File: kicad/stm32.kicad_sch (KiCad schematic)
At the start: 21 parts, among them U1 STM32L452REI6, X1 NX2012SA-32.768KHZ-EXS00A-MU0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

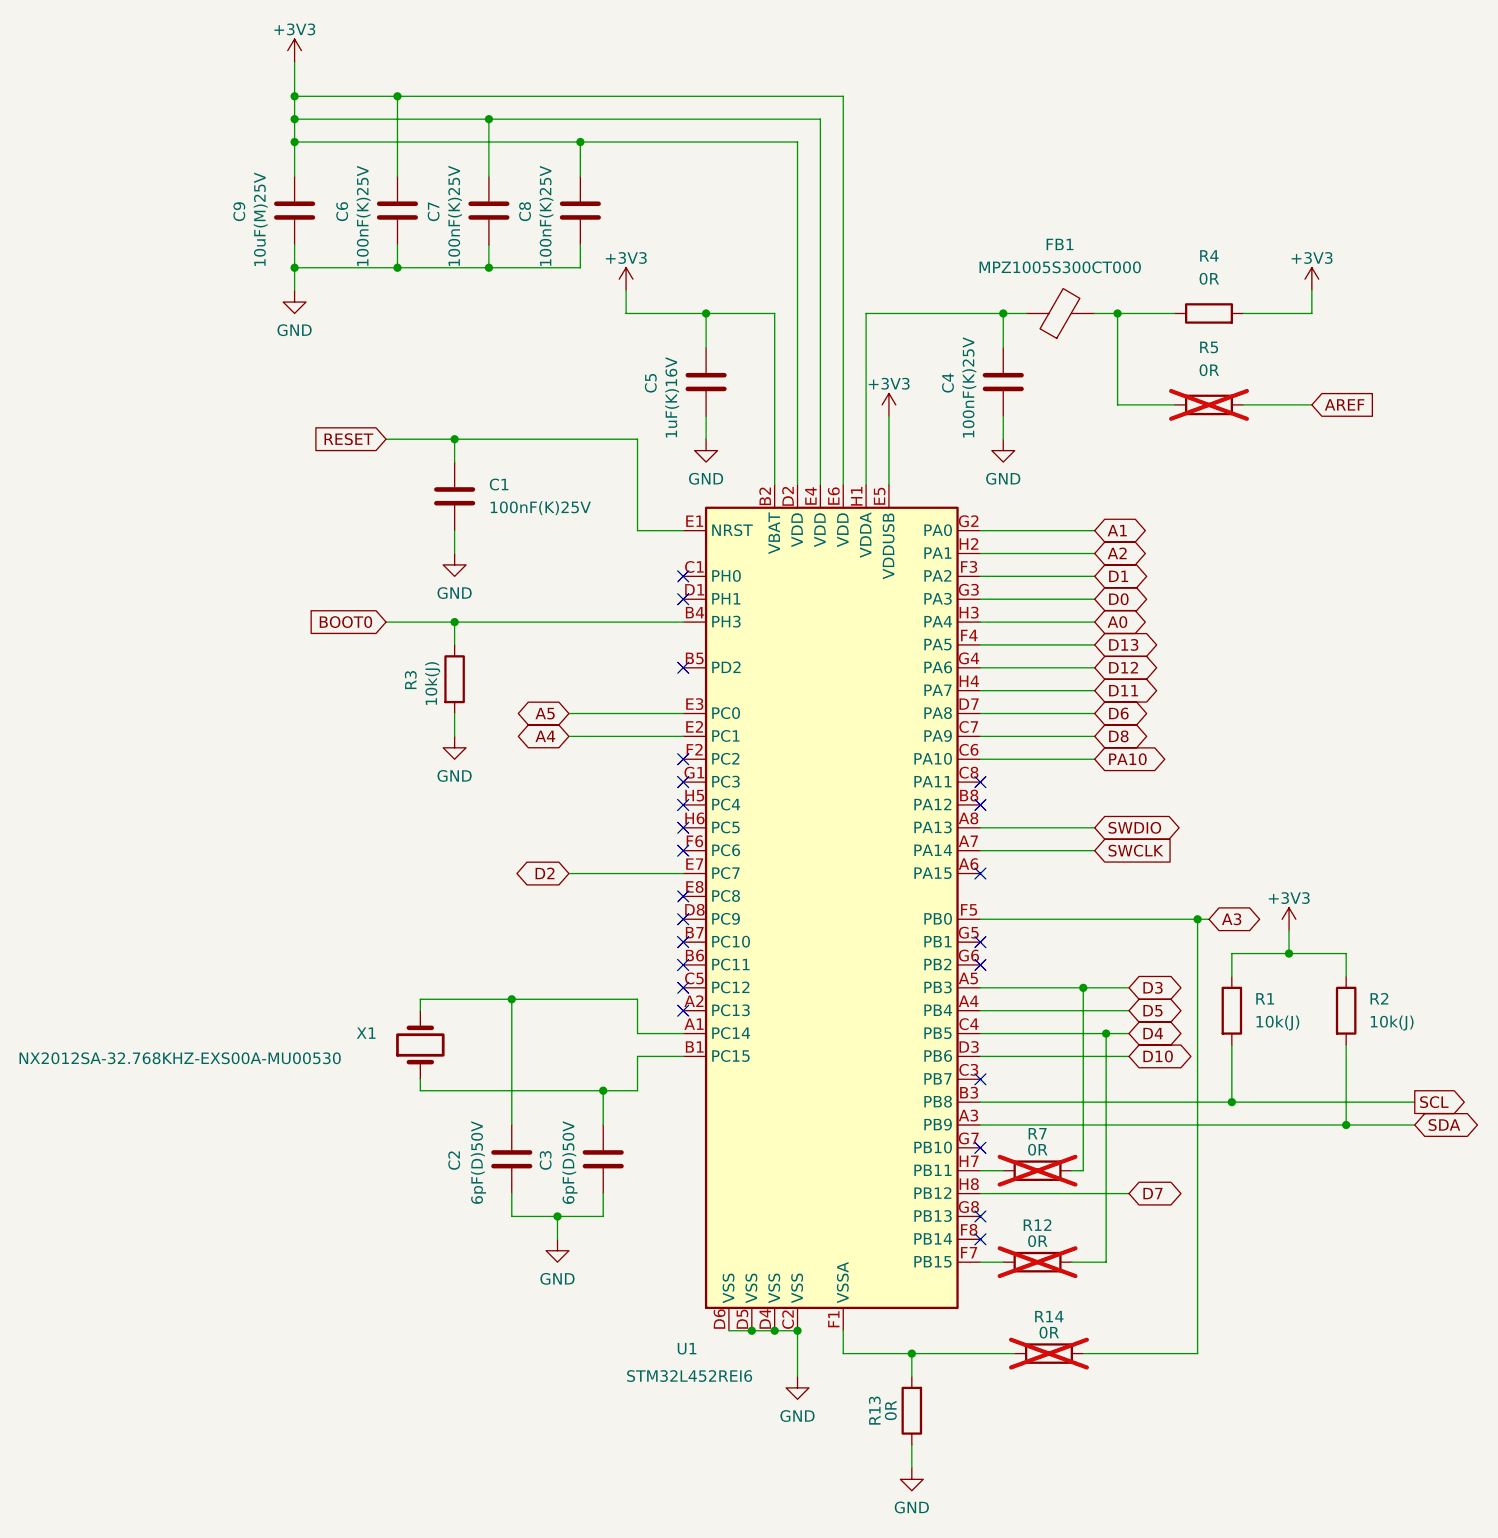
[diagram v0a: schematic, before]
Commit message: BOMを追加
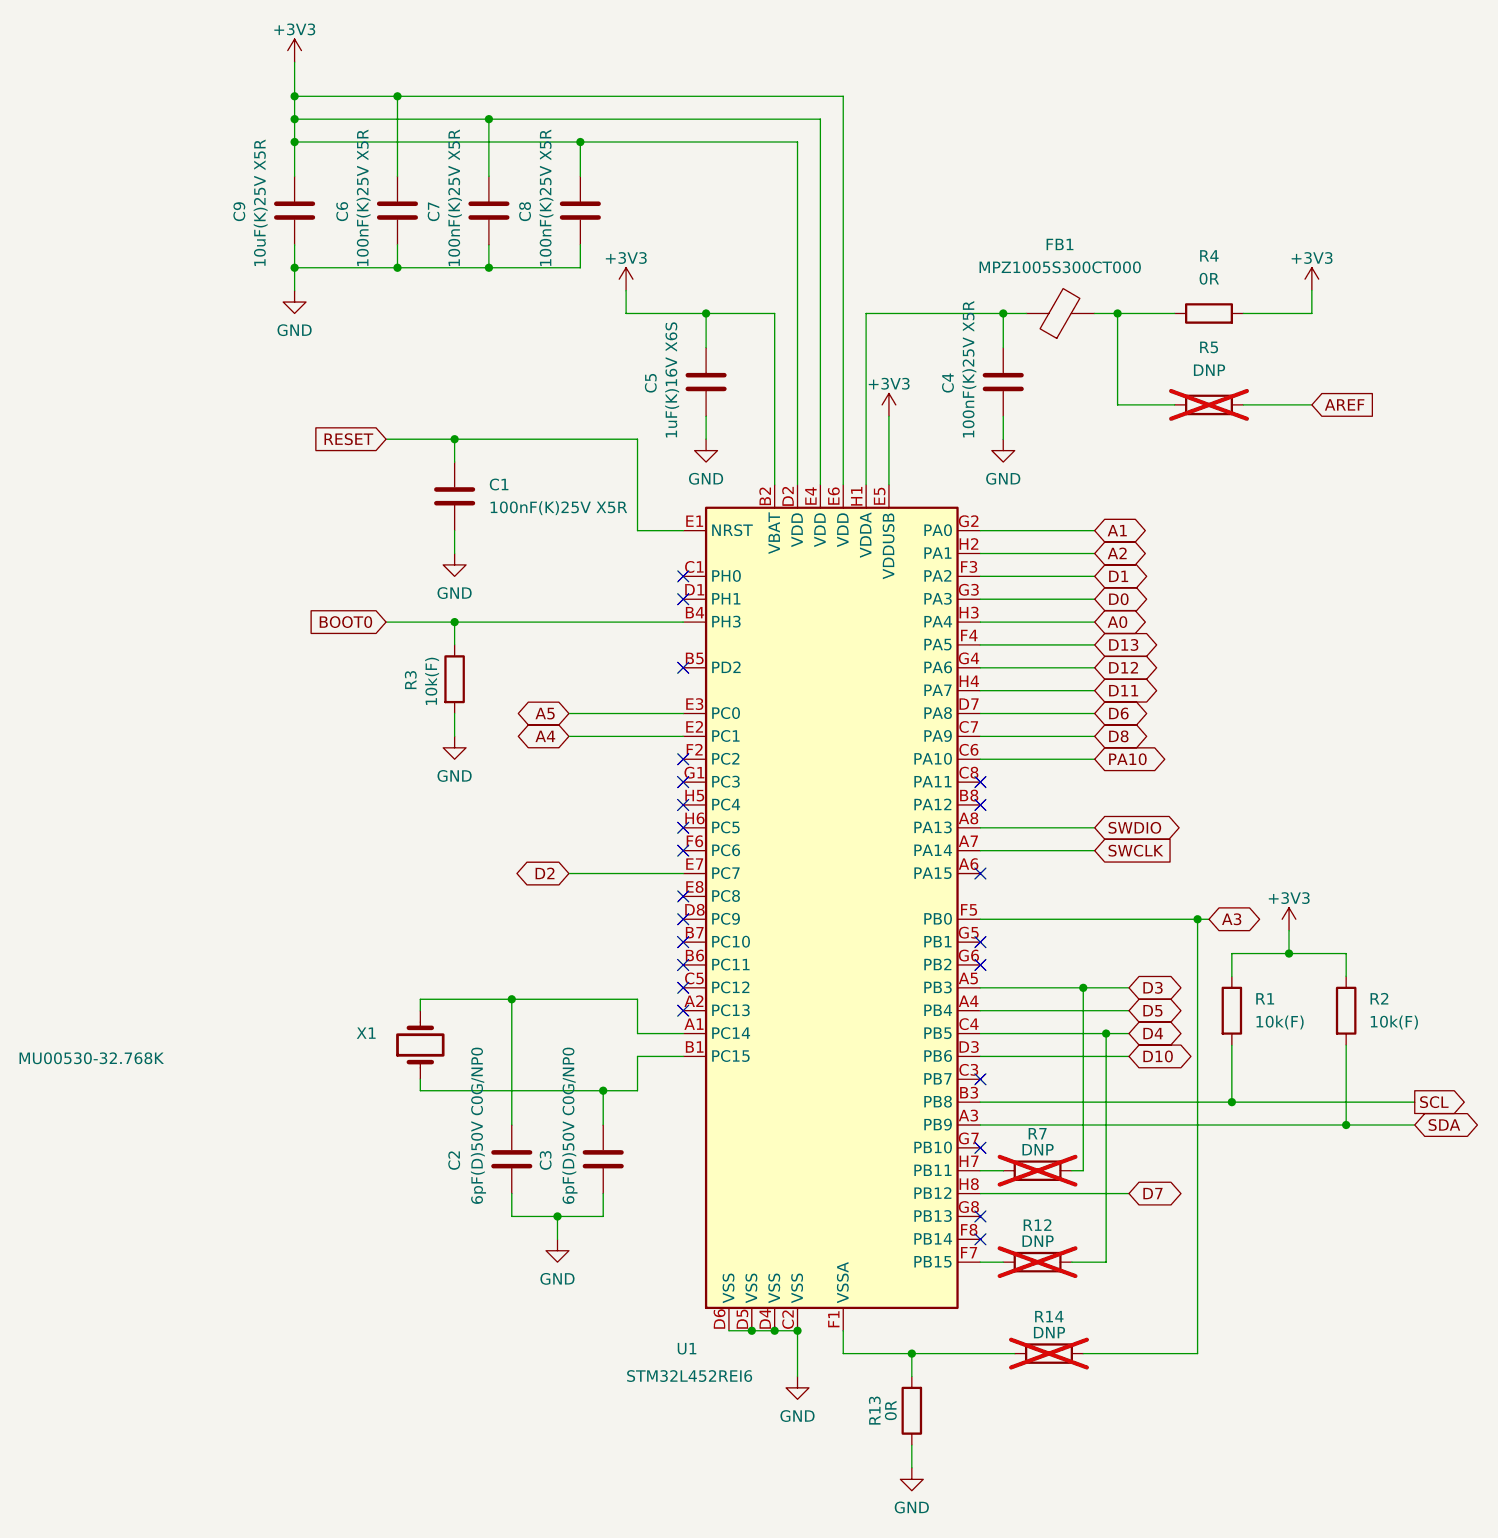
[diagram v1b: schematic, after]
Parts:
- C1, C4, C6, C7, C8: value 100nF(K)25V -> 100nF(K)25V X5R; MANUFACTURER (none) -> Murata Electronics; MPN (none) -> GRM033R61E104KE14D
- C2, C3: value 6pF(D)50V -> 6pF(D)50V C0G/NP0; MANUFACTURER (none) -> Murata Electronics; MPN (none) -> GRM1555C1H6R0DA01D
- C5: value 1uF(K)16V -> 1uF(K)16V X6S; MANUFACTURER (none) -> Murata Electronics; MPN (none) -> GRM155C81C105KE11D
- C9: value 10uF(M)25V -> 10uF(K)25V X5R; MANUFACTURER (none) -> Murata Electronics; MPN (none) -> GRM188R61E106KA73D
- FB1: MANUFACTURER (none) -> TDK Corporation; MPN (none) -> MPZ1005S300CT000
- R1, R2, R3: value 10k(J) -> 10k(F); MANUFACTURER (none) -> YAGEO; MPN (none) -> RC0402FR-0710KL
- R12, R14, R5, R7: value 0R -> DNP
- R13, R4: MANUFACTURER (none) -> YAGEO; MPN (none) -> RC0402JR-070RL
- U1: MANUFACTURER (none) -> STMicroelectronics; MPN (none) -> STM32L452REI6
- X1: value NX2012SA-32.768KHZ-EXS00A-MU00530 -> MU00530-32.768K; MANUFACTURER (none) -> NDK America, Inc.; MPN (none) -> MU00530-32.768K
